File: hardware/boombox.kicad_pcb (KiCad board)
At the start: 4 copper layers, 125 x 107.9 mm, 82 parts, among them J1 Micro_SD_Card_Det1, J2 Screw_Terminal_01x07, J4 USB_C_Receptacle_USB2.0_16P, J5 Screw_Terminal_01x07, U1 Pico, U10 MAX98365A, U2 TMAG5231, U3 TMAG5231, U4 TMAG5231, U5 TMAG5231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

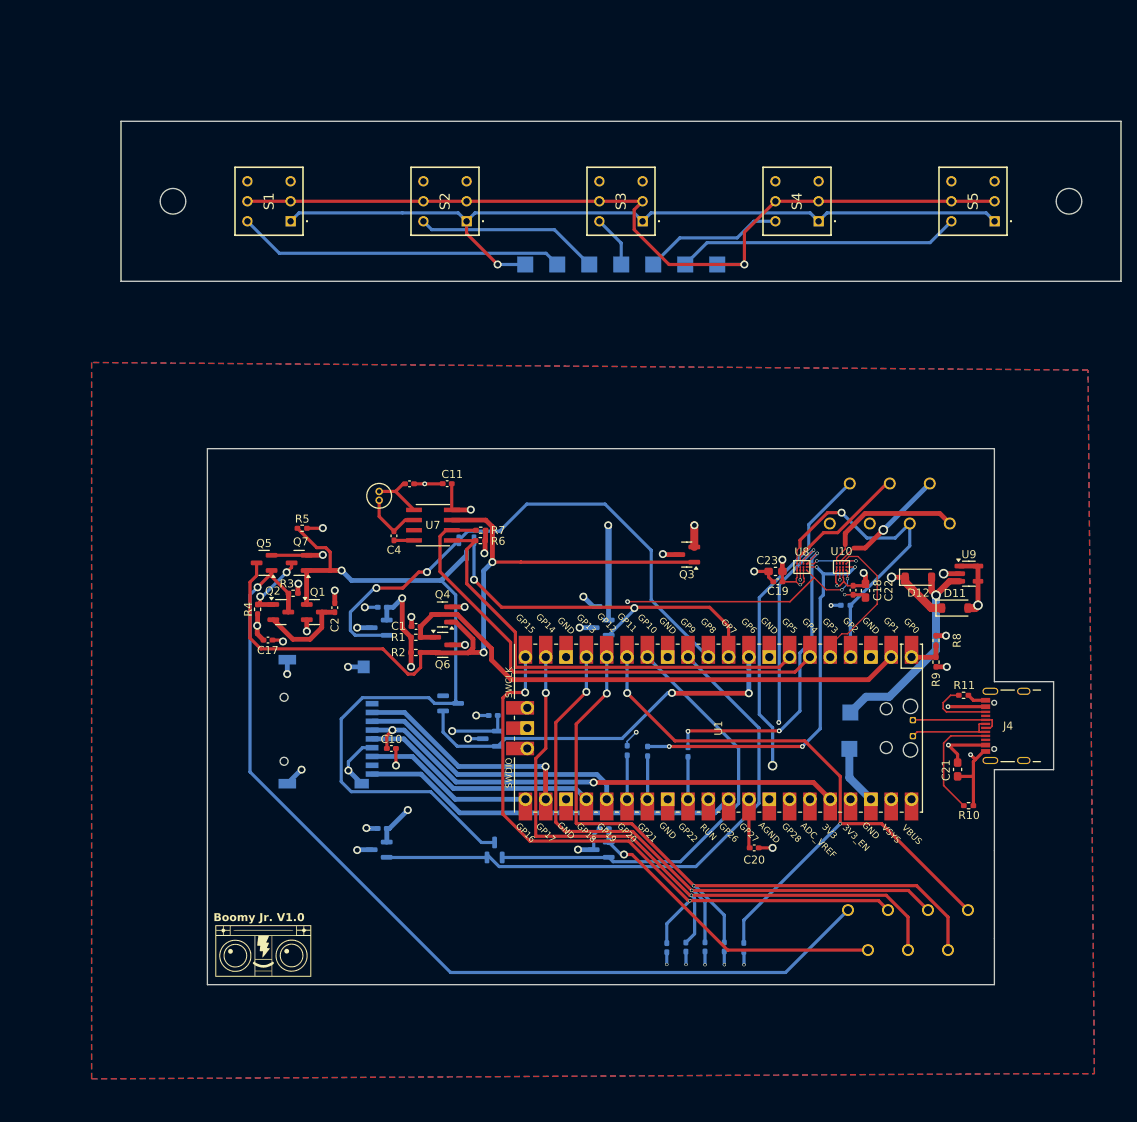
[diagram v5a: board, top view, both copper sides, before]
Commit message: Rounded corners
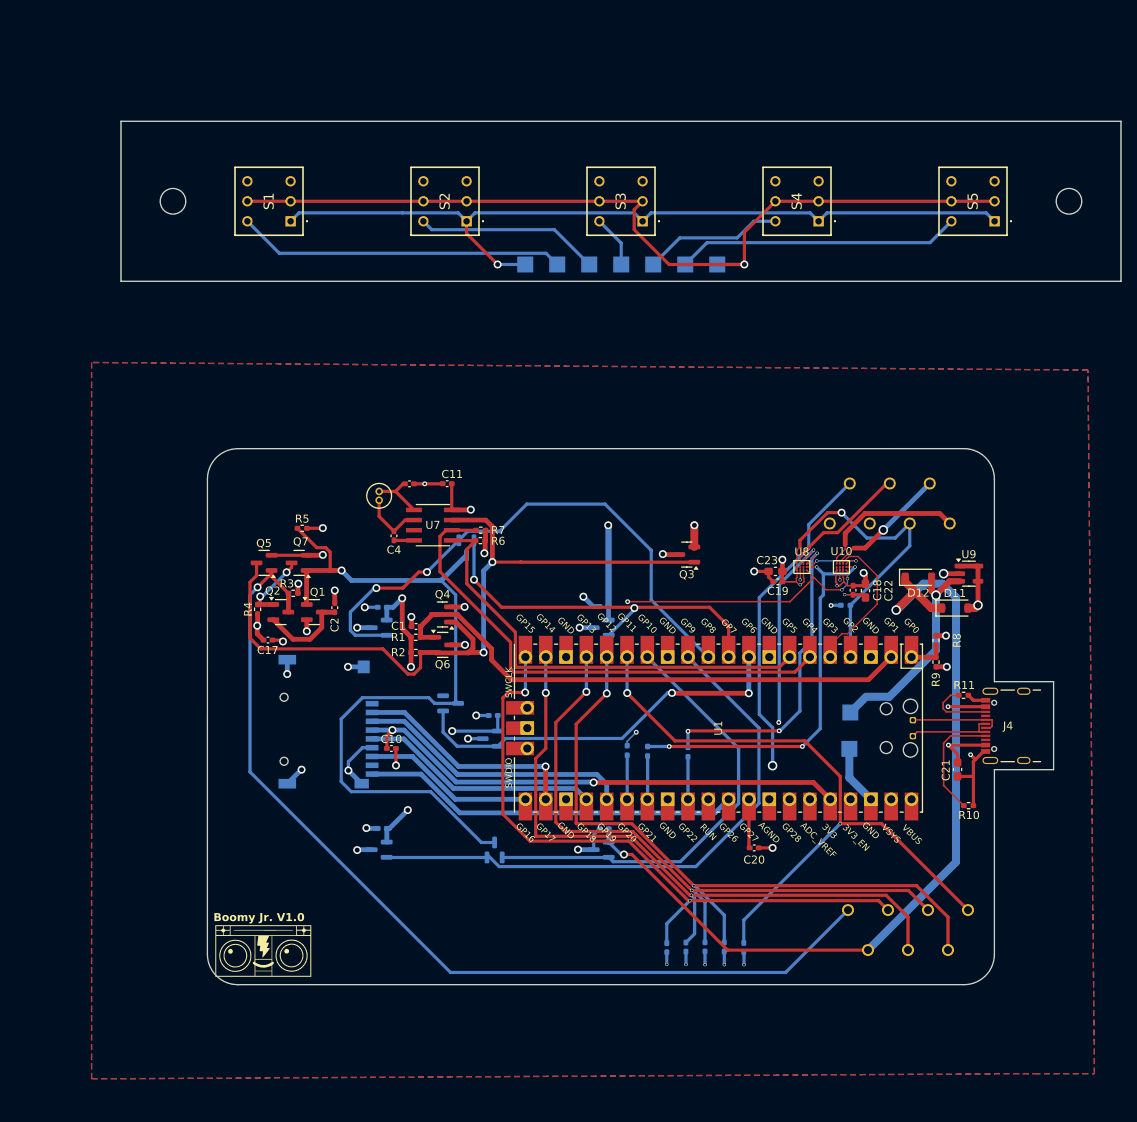
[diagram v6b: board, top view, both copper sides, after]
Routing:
- net SLP_PWR: track 250.2 -> 302.1 mm
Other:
- outline, holes or cut-outs redrawn
- board text added: "1"
- board text added: "2"
- board text added: "3"
- board text added: "4"
- board text added: "5"
- board text added: "6"
- board text added: "7"

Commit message: Reading from SD card
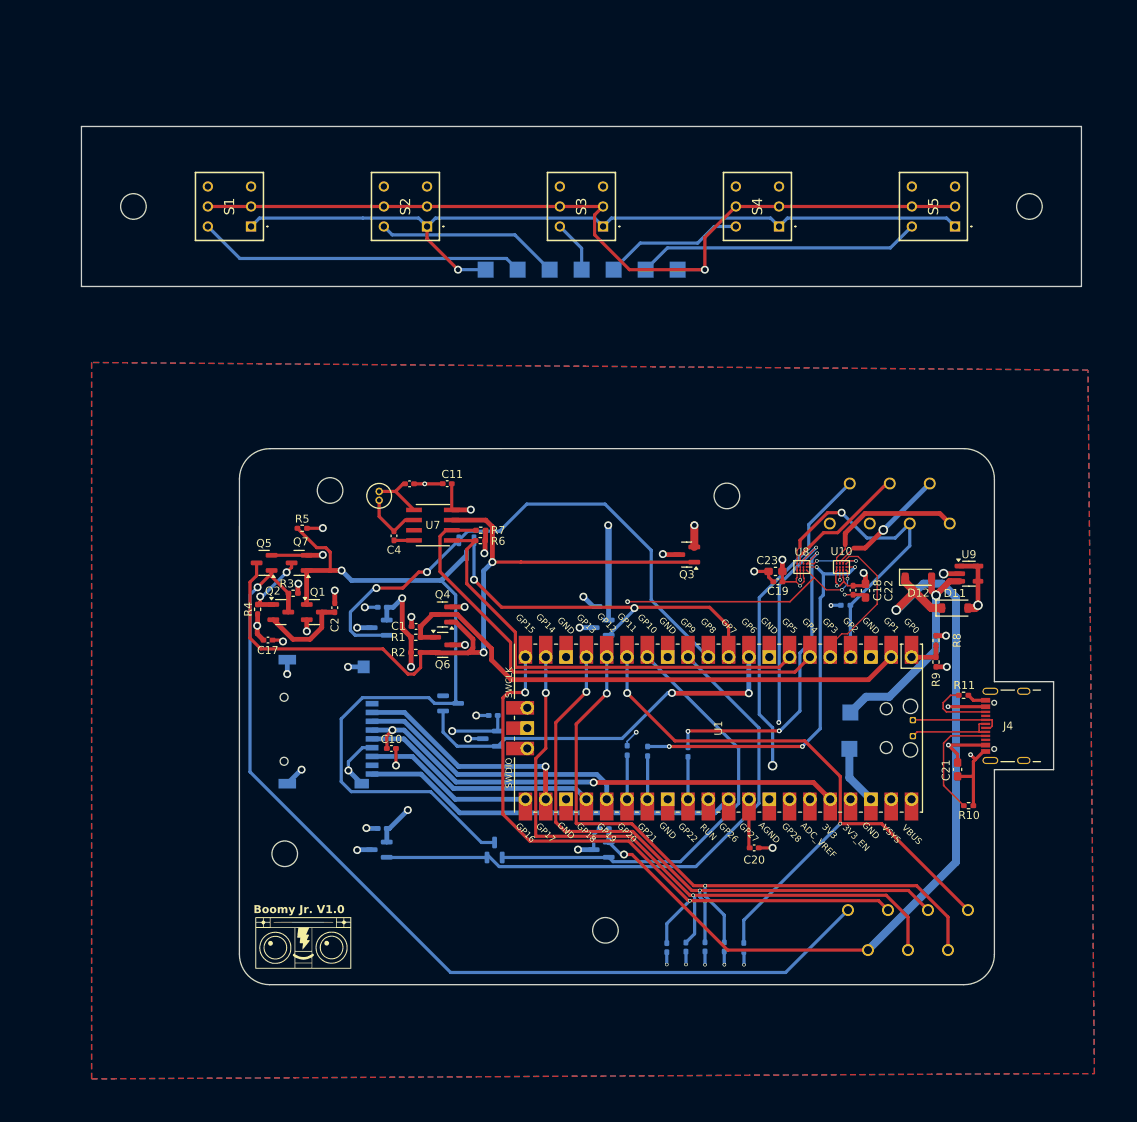
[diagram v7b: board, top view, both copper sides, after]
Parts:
- removed the REF** at (99.0, 36.4)
- removed the REF** at (211.0, 36.4)
- added REF**: MountingHole_3.2mm_M3, MountingHole:MountingHole_3.2mm_M3, F.Cu at (168.2, 73.2)
- added REF**: MountingHole_3.2mm_M3, MountingHole:MountingHole_3.2mm_M3, F.Cu at (94.0, 37.0)
- added REF**: MountingHole_3.2mm_M3, MountingHole:MountingHole_3.2mm_M3, F.Cu at (153.0, 127.5)
- added REF**: MountingHole_3.2mm_M3, MountingHole:MountingHole_3.2mm_M3, F.Cu at (112.9, 118.0)
- added REF**: MountingHole_3.2mm_M3, MountingHole:MountingHole_3.2mm_M3, F.Cu at (206.0, 37.0)
- added REF**: MountingHole_3.2mm_M3, MountingHole:MountingHole_3.2mm_M3, F.Cu at (118.6, 72.5)
- moved G*** 5.10 mm to (115.2, 129.1)
- moved TP1 4.99 mm to (142.1, 45.0)
- moved TP12 4.99 mm to (162.1, 45.0)
- moved TP2 4.99 mm to (146.1, 45.0)
- moved TP3 4.99 mm to (150.1, 45.0)
- moved TP4 4.99 mm to (154.1, 45.0)
- moved TP5 4.99 mm to (158.1, 45.0)
- moved TP8 4.99 mm to (138.1, 45.0)
- moved S1 4.99 mm to (106.0, 37.0)
- moved S2 4.99 mm to (128.0, 37.0)
- moved S3 4.99 mm to (150.0, 37.0)
- moved S4 4.99 mm to (172.0, 37.0)
- moved S5 4.99 mm to (194.0, 37.0)
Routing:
- net /Audio/HEADPHONE_EN: track 35.7 -> 36.7 mm
- net Net-(J2-Pin_6): track 86.6 -> 85.9 mm
- net Net-(J2-Pin_5): track 80.6 -> 80.1 mm
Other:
- board size 125 x 107.9 mm -> 125 x 107.3 mm

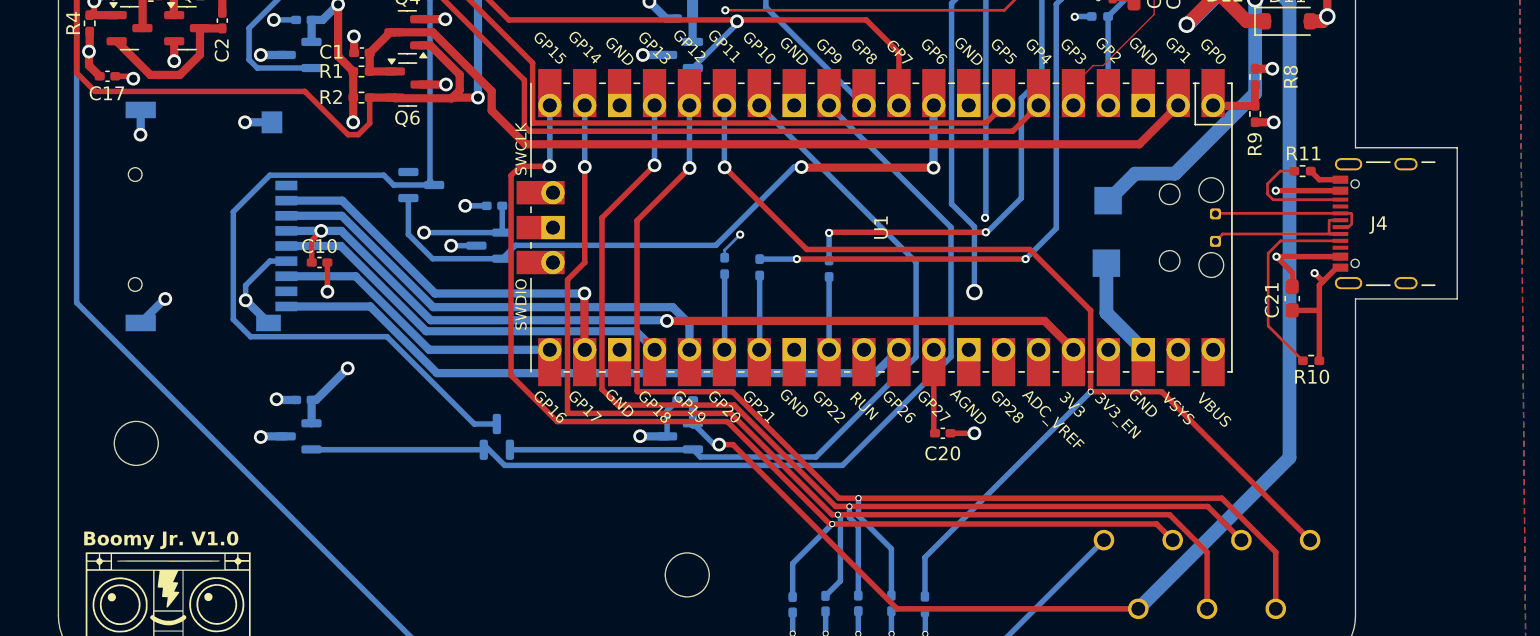
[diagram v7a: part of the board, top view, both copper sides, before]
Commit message: Flipped mosfet
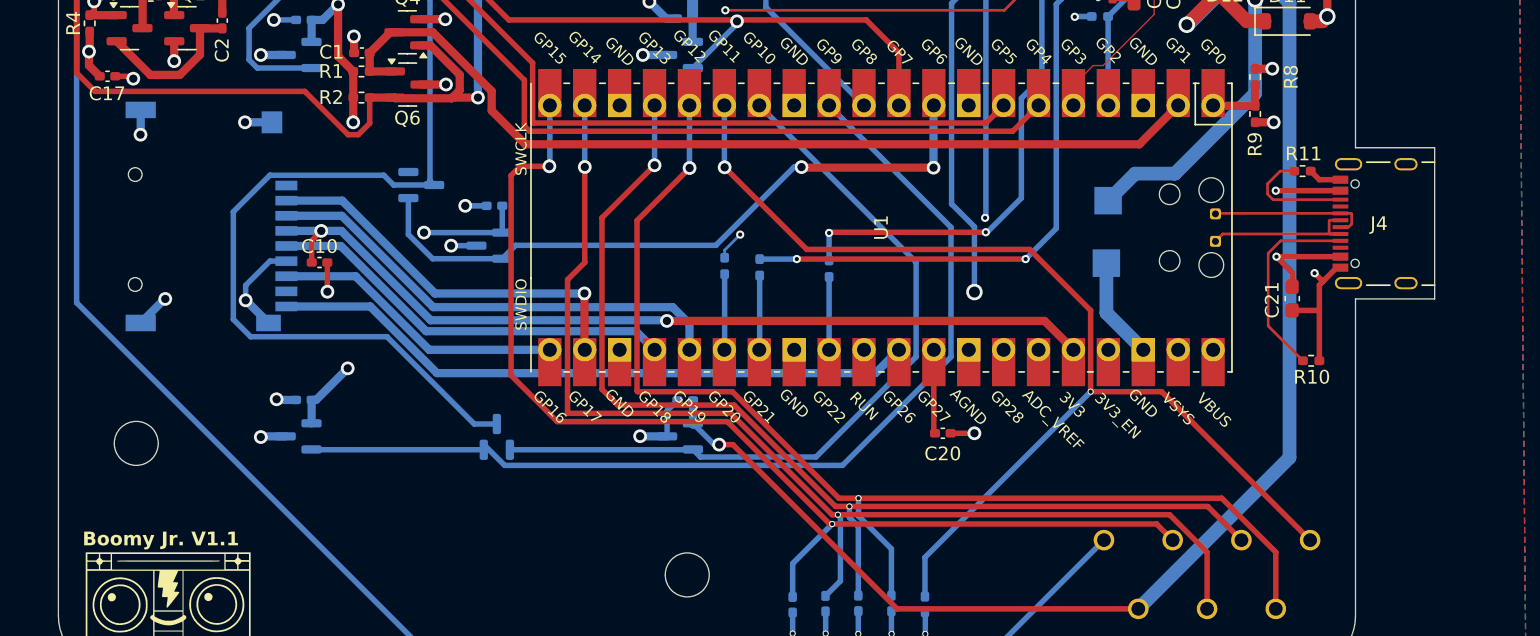
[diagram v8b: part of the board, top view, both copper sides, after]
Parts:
- C5, C6, C7, C8, C9: value .1u -> 0.1u
- R1, R2: value 3.3M -> 1M
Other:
- outline, holes or cut-outs redrawn
- board text added: "Boomy Jr. V1.1"
- board text removed: "Boomy Jr. V1.0"
